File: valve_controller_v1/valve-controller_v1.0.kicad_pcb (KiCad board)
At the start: 4 copper layers, 81 parts, among them J1 Solar Panel, J2 Solenoid #1,2 Output, J3 Solenoid #3,4 Output, J4 USB_C_Receptacle_USB2.0_16P, J5 Debug & Program, J6 Debug, Q1 AO3401A, Q3 AP2003, SW1 XKB5858, SW2 Reset, SW3 Boot Selector, SW4 Voltage Selector, U1 BQ21040DBV, U10 DRV8231ADSG, U2 XC6220B331MR, U3 CH340E, U4 RAK3172-xx-9-SM-xI, U5 LT218, U6 LMR62421XMF, U7 DRV8231ADSG, U8 DRV8231ADSG, U9 DRV8231ADSG

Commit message: Routed PCB and added 3D models
Routed the entire PCB
Added 3D Models for the RAK module and Battery Holder
Improved Silkscreen
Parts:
- removed TP10: BAT_MON, TestPoint:TestPoint_Pad_D1.0mm
- removed TP11: RAK_PWR_EN, TestPoint:TestPoint_Pad_D1.0mm
- C12: footprint Capacitor_THT:CP_Radial_D18.0mm_P7.50mm -> Capacitor_THT:CP_Radial_D16.0mm_P7.50mm
- H1, H2, H3, H4: footprint MountingHole:MountingHole_2.2mm_M2 -> MountingHole:MountingHole_2.5mm
- JP1: moved to B.Cu
- SW4: footprint Package_SO:SO-4_4.4x4.3mm_P2.54mm -> Button_Switch_SMD:SW_DIP_SPSTx02_Slide_Omron_A6H-2101_W6.15mm_P1.27mm
- TP9: value ~{BAT_MON_EN} -> RAK_PWR_EN
- moved J2 241.9 mm to (93.0, 133.2)
- moved R22 231.9 mm to (96.3, 110.0), turned to -90 degrees
- moved R12 231.5 mm to (73.7, 50.5)
- moved C8 231.3 mm to (75.7, 50.5)
- moved R23 230.3 mm to (75.3, 110.0), turned to -90 degrees
- moved U9 230.2 mm to (94.1, 110.0), turned to -90 degrees
- moved SW3 230.1 mm to (51.6, 52.3)
- moved U10 228.5 mm to (73.1, 110.0), turned to -90 degrees
- moved SW2 226.1 mm to (74.7, 47.0)
- moved J6 224.5 mm to (68.3, 79.2), turned to 180 degrees
- moved J3 222.6 mm to (85.0, 118.0), turned to -90 degrees
- moved J5 220.6 mm to (80.8, 48.8), turned to -90 degrees
- moved R20 219.9 mm to (106.7, 110.0), turned to -90 degrees
- moved C6 218.7 mm to (86.4, 55.0)
- moved U4 218.7 mm to (75.9, 62.5)
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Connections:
- J2 pad 1: /Valve Driver/S1_O1 -> /Valve Driver/S1_O2
- J2 pad 2: /Valve Driver/S1_O2 -> /Valve Driver/S1_O1
- J2 pad 3: /Valve Driver/S2_O1 -> /Valve Driver/S2_O2
- J2 pad 4: /Valve Driver/S2_O2 -> /Valve Driver/S2_O1
- J3 pad 1: /Valve Driver/S3_O1 -> /Valve Driver/S3_O2
- J3 pad 2: /Valve Driver/S3_O2 -> /Valve Driver/S3_O1
- J3 pad 3: /Valve Driver/S4_O1 -> /Valve Driver/S4_O2
- J3 pad 4: /Valve Driver/S4_O2 -> /Valve Driver/S4_O1
- TP9 pad 1: /MCU/~{BAT_MON_EN} -> /MCU/RAK_PWR_EN
- U4 pad 10: unconnected-(U4-PA11/SDA-Pad10) -> /MCU/RAK_CTRL_S4_I1
- U4 pad 13: /MCU/RAK_CTRL_S2_I2 -> /MCU/RAK_CTRL_S3_I1
- U4 pad 14: /MCU/RAK_CTRL_S2_I1 -> /MCU/RAK_CTRL_S3_I2
- U4 pad 15: /MCU/RAK_CTRL_S1_I2 -> /MCU/RAK_CTRL_S2_I1
- U4 pad 16: /MCU/RAK_CTRL_S1_I1 -> /MCU/RAK_CTRL_S2_I2
- U4 pad 19: /MCU/RAK_CTRL_S3_I2 -> /MCU/RAK_CTRL_S1_I1
- U4 pad 20: /MCU/RAK_CTRL_S4_I1 -> /MCU/RAK_CTRL_S1_I2
- U4 pad 25: /MCU/RAK_CTRL_S4_I2 -> unconnected-(U4-PA10/PIN_A3-Pad25)
- U4 pad 26: /MCU/~{BAT_MON_EN} -> unconnected-(U4-PB2/PIN_A2-Pad26)
- U4 pad 31: unconnected-(U4-PB4/PIN_A1-Pad31) -> /MCU/BAT_MON
- U4 pad 32: /MCU/BAT_MON -> /MCU/~{BAT_MON_EN}
- U4 pad 6: /MCU/RAK_CTRL_S3_I1 -> unconnected-(U4-PA1-Pad6)
- U4 pad 9: unconnected-(U4-PA12/SCL-Pad9) -> /MCU/RAK_CTRL_S4_I2
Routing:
- net VDD: track 15.3 -> 110.7 mm, vias 0 -> 4
- net VBUS: track 0.00 -> 71.6 mm, vias 0 -> 2
- net VCC: track 4.91 -> 72.6 mm, vias 0 -> 11
- net /MCU/RAK_CTRL_S1_I2: track 0.00 -> 58.3 mm
- net /MCU/RAK_CTRL_S1_I1: track 0.00 -> 53.1 mm
- net /MCU/RAK_CTRL_S4_I2: track 0.00 -> 47.5 mm
- net /MCU/RAK_CTRL_S4_I1: track 0.00 -> 46.7 mm
- net /MCU/RAK_CTRL_S2_I1: track 0.00 -> 46.1 mm
- net /MCU/RAK_CTRL_S2_I2: track 0.00 -> 45.8 mm
- net /MCU/RAK_CTRL_S3_I1: track 0.00 -> 44.4 mm
- net /MCU/RAK_CTRL_S3_I2: track 0.00 -> 44.3 mm, vias 0 -> 1
- net +BATT: track 4.68 -> 47.0 mm, vias 0 -> 28
- net /MCU/~{RAK_RST}: track 0.00 -> 34.3 mm
- net /MCU/RAK_BOOT: track 0.00 -> 33.5 mm, vias 0 -> 2
- net /MCU/RAK_SWDIO: track 0.00 -> 30.6 mm, vias 0 -> 2
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- added copper zone on In1.Cu, net +3V3
- added copper zone on F.Cu, net +BATT
- added copper zone on In1.Cu, net +BATT
- added copper zone on B.Cu, net GND
- added copper zone on F.Cu, net GND
- added copper zone on F.Cu, net VS
- added copper zone on In2.Cu, net VS
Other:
- board outline added: 78 x 110 mm
- board text added: "14V 9V"
- board text added: "BATTERY POLARITY"
- board text added: "BOOT (0|1)"
- board text added: "DEBUG"
- board text added: "ON/OFF"
- board text added: "PROG"
- board text added: "RESET"
- board text added: "RX TX GND"
- board text added: "SOLAR PANEL"
- board text added: "TP1"
- board text added: "TP1 - Vcc TP2 - Vbat TP3 - Reg. Enable TP4 - 3V3 TP5 - Bat. Mon. Enable TP6 - Bat. Mon. TP7 - TX TP8 - RX TP9 - RAK Pwr. Enable"
- board text added: "TP2"
- board text added: "TP3"
- board text added: "TP4"
- board text added: "TP5"
- board text added: "TP6"
- board text added: "TP7"
- board text added: "TP8"
- board text added: "TP9"

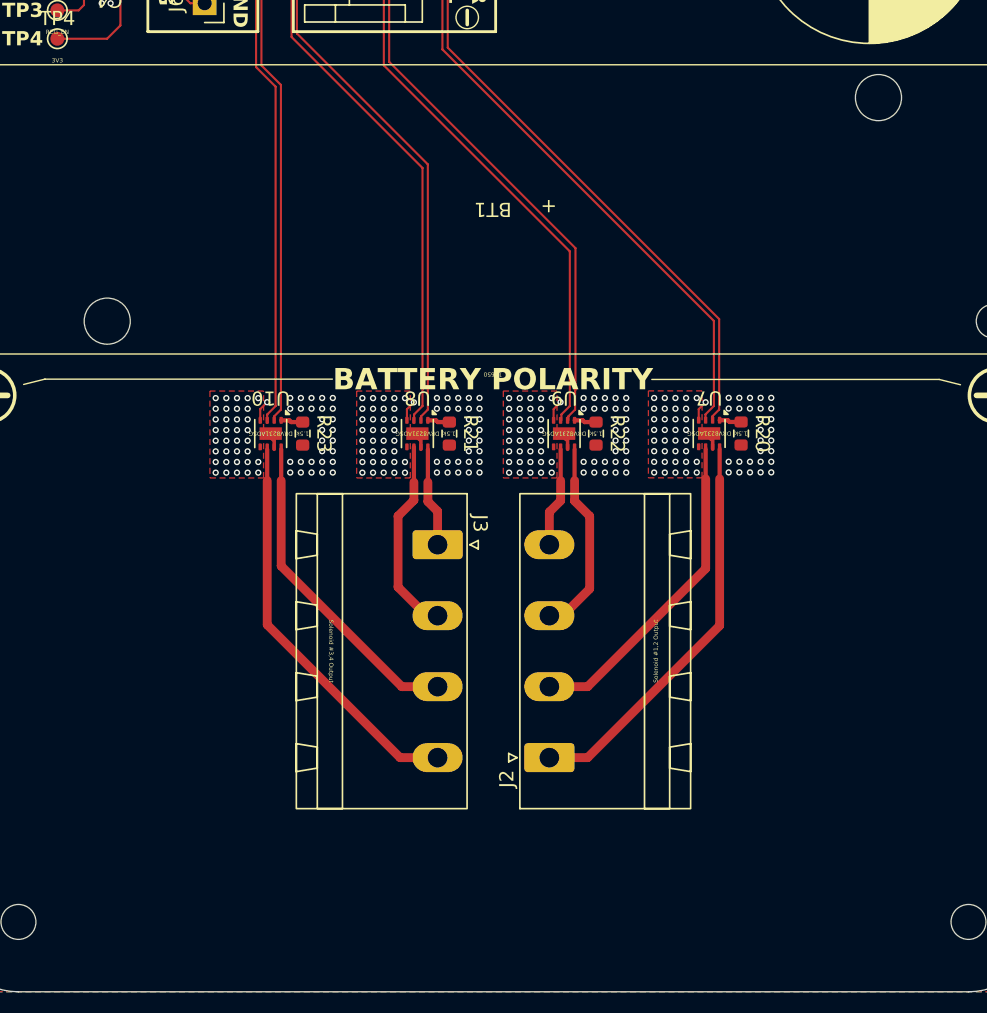
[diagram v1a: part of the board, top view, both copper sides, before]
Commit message: Created output connector footprint
Created output connector footprint based on the datasheet (Added both parts of the connector, the one soldered to the PCB and the oen that is connected to it)
Added 3D models of both parts and assigned them to the footprint
Relocated the connectors to avoid colission with other components
Rerouted the connectors
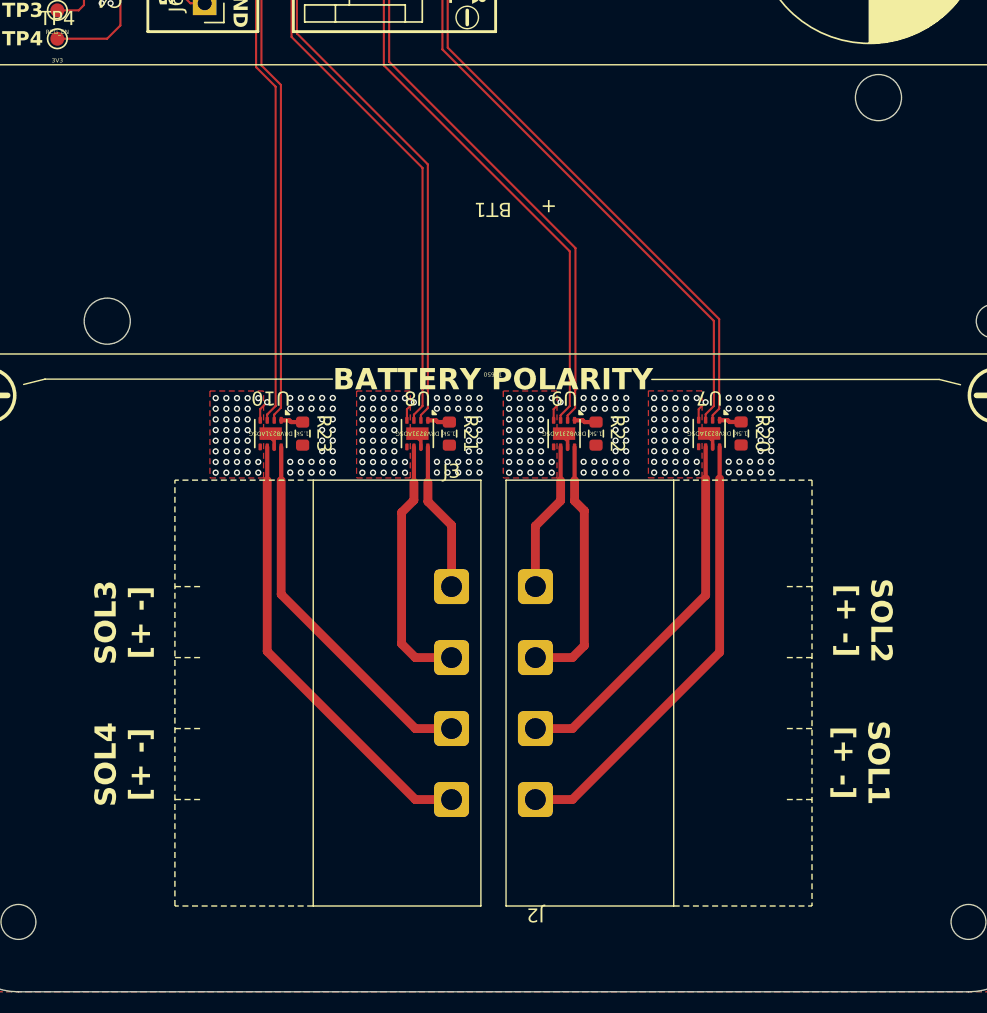
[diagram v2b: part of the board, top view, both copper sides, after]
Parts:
- J2, J3: footprint Connector_Phoenix_MSTB:PhoenixContact_MSTBA_2,5_4-G-5,08_1x04_P5.08mm_Horizontal -> Wisflow:2EDGRM-5.08-04P
- moved J3 10.7 mm to (86.0, 128.6), turned to 0 degrees
- moved J2 4.73 mm to (92.0, 128.6), turned to 180 degrees
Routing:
- net /Valve Driver/S3_O1: track 14.2 -> 18.4 mm
- net /Valve Driver/S2_O2: track 14.1 -> 18.4 mm
- net /Valve Driver/S4_O2: track 23.1 -> 26.7 mm
- net /Valve Driver/S3_O2: track 7.11 -> 10.7 mm
- net /Valve Driver/S2_O1: track 7.16 -> 10.7 mm
- net /Valve Driver/S1_O2: track 28.7 -> 32.3 mm
- net /Valve Driver/S4_O1: track 28.7 -> 32.2 mm
- net /Valve Driver/S1_O1: track 23.2 -> 26.8 mm
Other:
- board text added: "SOL1 [+ -]"
- board text added: "SOL2 [+ -]"
- board text added: "SOL3 [+ -]"
- board text added: "SOL4 [+ -]"

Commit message: Added logo and minor footprint location corrections
Added Wisflow Logo on front silkscreen
Added logo, revision and serial number text on the back silkscreen
Added jumper description on the back silkscreen
Corrected battery holder and capacitor location to avoid colision with the case (middle screw boss)
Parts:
- added LG1: ~, Wisflow:WisflowLogo_30mm, F.Cu at (89.0, 147.0)
- added LG2: ~, Wisflow:WisflowLogo_20mm, B.Cu at (89.1, 91.7)
- moved TP3 3.24 mm to (54.6, 80.4)
- moved TP4 2.90 mm to (60.3, 80.4)
- moved BT1 1.50 mm to (89.0, 92.5)
- moved C12 1.00 mm to (112.2, 73.0)
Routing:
- net +3V3: track 32.6 -> 28.8 mm
- net /Power/REG_EN: track 20.8 -> 23.4 mm
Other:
- board text added: "Close - VCC prog internal 3V3 Open - VCC prog floating"
- board text added: "Rev 1.0"
- board text added: "SN:"
- board text added: "Wisflow Valve Controller"

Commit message: Final corrections for manufacturing
Created new condenser footprint to better represent the actual position
Created new voltage selector ip switch footprint
Selected bigger footprint for R19 (was 1206 now is 2512 as in the legacy version)
Corrected D5 footprint (was SOD-123 now is SMA)
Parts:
- C12: footprint Capacitor_THT:CP_Radial_D16.0mm_P7.50mm -> Wisflow:CP_Horizontal_D16_L25_P7.5mm
- D5: footprint Diode_SMD:D_SC-80 -> Diode_SMD:D_SMA
- J1: footprint Connector_JST:JST_EH_S2B-EH_1x02_P2.50mm_Horizontal -> Connector_JST:JST_PH_S2B-PH-SM4-TB_1x02-1MP_P2.00mm_Horizontal
- R19: footprint Resistor_SMD:R_1206_3216Metric -> Resistor_SMD:R_2512_6332Metric
- SW4: footprint Button_Switch_SMD:SW_DIP_SPSTx02_Slide_Omron_A6H-2101_W6.15mm_P1.27mm -> Wisflow:SMXMS-02
- moved C11 6.36 mm to (101.6, 77.4), turned to 90 degrees
- moved C12 5.93 mm to (115.2, 78.1)
- moved C13 4.18 mm to (91.9, 77.4)
- moved J1 3.78 mm to (80.7, 76.7), turned to 90 degrees
- moved D5 2.83 mm to (94.2, 73.1), turned to 180 degrees
- moved R19 1.71 mm to (96.7, 77.4)
- moved SW4 0.69 mm to (101.8, 62.8), turned to 0 degrees
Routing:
- net VCC: track 72.6 -> 80.0 mm, vias 11 -> 14
- net Net-(D5-K): track 15.3 -> 20.6 mm
- net VS: track 3.92 -> 6.16 mm, vias 142 -> 143
- net unconnected-(U4-PA1-Pad6): track 1.56 -> 0.00 mm, vias 1 -> 0
- net Net-(D5-A): track 5.83 -> 7.26 mm
- net Net-(U6-FB): track 17.8 -> 18.8 mm
- net GND: track 19.1 -> 19.3 mm, vias 184 -> 183
- net /MCU/RAK_CTRL_S3_I2: vias 1 -> 0
- net +BATT: vias 28 -> 27

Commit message: Added user LED
Added missing user LED. (This LED was present in V0.3c but is missin gin V1.0)
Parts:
- added D6: Blue, LED_SMD:LED_0603_1608Metric, F.Cu at (52.8, 80.0)
- added R24: 1k, Resistor_SMD:R_0603_1608Metric, F.Cu at (56.0, 80.0)
- moved TP3 71.4 mm to (125.6, 72.3)
- moved TP4 65.3 mm to (125.6, 78.1)
- moved TP2 0.09 mm to (105.2, 43.8)
- moved TP1 0.09 mm to (105.2, 41.7)
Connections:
- C2 pad 1: VDD -> VCC
- D3 pad 2: VCC -> V_{SOLAR}
- J1 pad 1: VCC -> V_{SOLAR}
- R3 pad 1: VDD -> VCC
- U2 pad 1: VDD -> VCC
- U4 pad 25: unconnected-(U4-PA10/PIN_A3-Pad25) -> /MCU/RAK_LED
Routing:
- net VDD: track 110.7 -> 27.3 mm, vias 4 -> 0
- net /Power/REG_EN: track 23.4 -> 95.0 mm, vias 0 -> 2
- net +3V3: track 28.8 -> 92.7 mm, vias 10 -> 11
- net V_{SOLAR}: track 0.00 -> 56.9 mm, vias 0 -> 8
- net /MCU/RAK_LED: track 0.00 -> 44.5 mm, vias 0 -> 2
- net VCC: track 80.0 -> 100.2 mm, vias 14 -> 5
- net Net-(D6-A): track 0.00 -> 1.63 mm
